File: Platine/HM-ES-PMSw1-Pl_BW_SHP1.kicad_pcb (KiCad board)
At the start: 2 copper layers, 23.2 x 20.7 mm, 13 parts, among them J11 BW_Gosund_Con, J4 Reset, U1 ATMEGA644PA-AU, U2 CC1101, Y1 Resonator

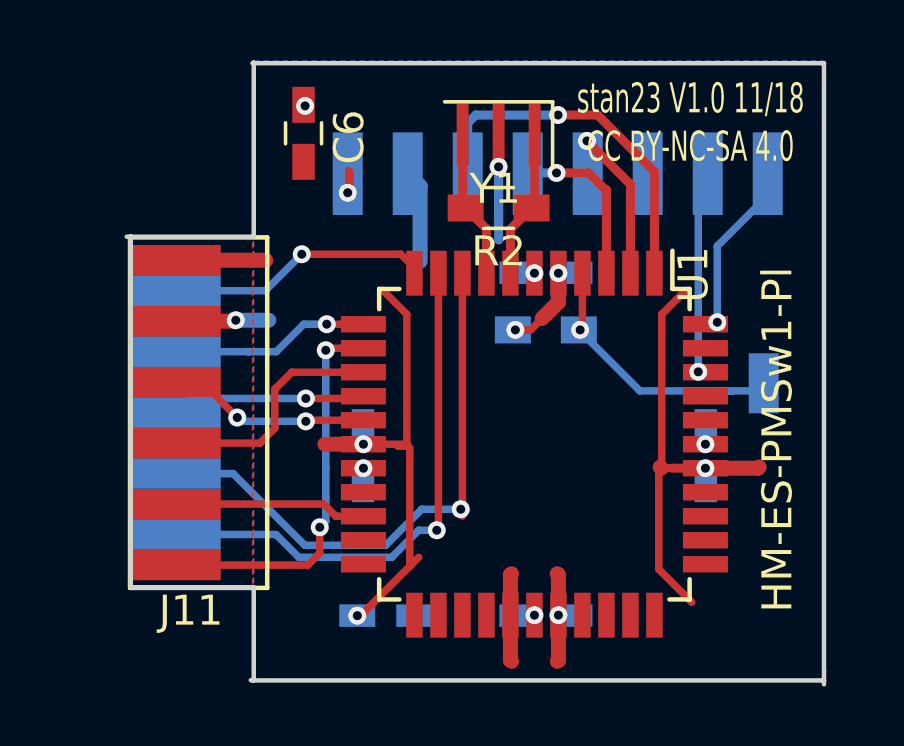
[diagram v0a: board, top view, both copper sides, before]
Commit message: Support for Gosund SP1 V2.3 (new WiFi module)
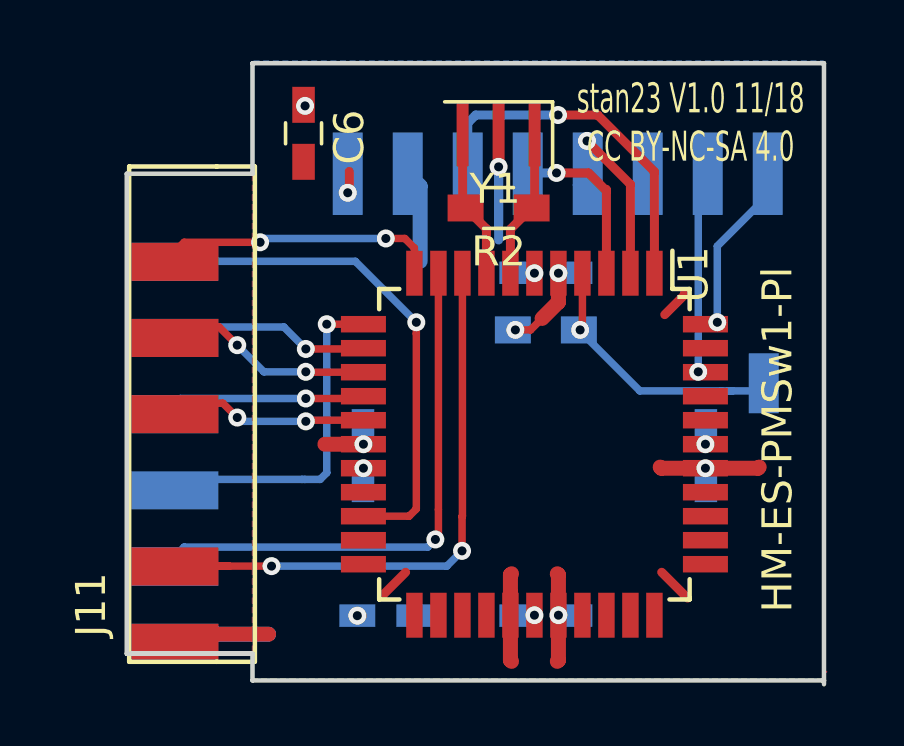
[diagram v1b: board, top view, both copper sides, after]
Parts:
- J11: footprint BW-SHP2:Gosund_SP1-C_V2.3 -> BW-SHP2:BW-SHP2-Con
- moved J11 6.53 mm to (96.6, 103.9)
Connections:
- J11 pad bLED: /LED_blue -> (no net)
- J11 pad rLED: /LED_red -> (no net)
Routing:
- net VCC: track 49.9 -> 22.9 mm
- net /SEL: track 6.42 -> 17.1 mm, vias 0 -> 1
- net /RELAY: track 13.6 -> 6.59 mm, vias 2 -> 1
- net /CF: track 6.69 -> 11.3 mm
- net (no net): track 0.00 -> 3.28 mm
- net /RX: track 19.1 -> 21.1 mm, vias 1 -> 2
- net /TX: track 18.4 -> 17.8 mm
- net /CF1: track 8.82 -> 9.10 mm, vias 1 -> 2
- net /BUTTON: track 8.00 -> 8.21 mm, vias 0 -> 2
- net GND: track 15.4 -> 15.5 mm, vias 7 -> 6
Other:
- outline, holes or cut-outs redrawn
